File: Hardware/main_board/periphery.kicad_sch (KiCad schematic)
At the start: 0 parts

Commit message: sch: done periphery
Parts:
- added C80: 100nF, symbol Device:C
- added C81: TBD, symbol Device:C_Polarized_US
- added D10: LED_ABGR, symbol Device:LED_ABGR
- added D11, D12, D13, D14, D15, D16, D17, D18, D19, D20, D21, D22, D23, D24, D25, D26, D27, D28, D29, D30, D31: TVS, symbol Device:D_TVS
- added D32: 1N4148, symbol Device:D
- added F1: 2A, symbol Device:Polyfuse
- added J4: SD, symbol Connector:Micro_SD_Card_Det1
- added J5: EXT0, symbol Connector_Generic:Conn_01x08
- added J6: EXT1, symbol Connector_Generic:Conn_01x10
- added J7: NFC, symbol Connector_Generic_MountingPin:Conn_01x18_MountingPin
- added R36, R37, R43, R44, R45, R46, R47: 47K, symbol Device:R_US
- added R38, R39: 150R, symbol Device:R_US
- added R40, R41, R42, R49: 51R, symbol Device:R_US
- added R48: 0R, symbol Device:R_US
- added R50: 1K, symbol Device:R_US
- added RN1, RN2, RN3, RN4: 51R, symbol Library:R_Park
- added TP34: SWCLK, symbol Connector:TestPoint
- added TP35: SWDIO, symbol Connector:TestPoint
- added TP36: UART1_TX, symbol Connector:TestPoint
- added TP37: UART1_RX, symbol Connector:TestPoint
- added TP38: I2C2_SCL, symbol Connector:TestPoint
- added TP39: I2C2_SDA, symbol Connector:TestPoint
- added TP40: RFID_C, symbol Connector:TestPoint
- added TP41: IR_RX, symbol Connector:TestPoint
- added TP42: IR_TX, symbol Connector:TestPoint
- added TP43: SP, symbol Connector:TestPoint
- added TP44: iBTN, symbol Connector:TestPoint
- added TP45: RFID_O, symbol Connector:TestPoint
- added TP46: RFID_P, symbol Connector:TestPoint
- added TP47: VIBRO, symbol Connector:TestPoint
- added TP48: NFC_CS, symbol Connector:TestPoint
- added TP49: RFID_I, symbol Connector:TestPoint
- added U11: LP5562TMX, symbol Library:LP5562TMX
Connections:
- new net: J4.3 (CMD), R40.2
- new net: J4.1 (DAT2), R37.1
- new net: J4.2 (DAT3/CD), R39.2
- new net: D16.1 (A1), J4.4 (VDD), R36.2, R37.2, R43.2, R44.2, R45.2, R46.2, R47.2, R48.2
- new net: J4.5 (CLK), R41.2
- new net: J4.7 (DAT0), R42.2
- new net: J4.8 (DAT1), R36.1
- new net: J4.9 (DET), R38.2
- new net: J6.2 (Pin_2), RN3.3
- new net: J6.3 (Pin_3), RN3.2
- new net: J6.5 (Pin_5), RN3.1
- new net: J6.6 (Pin_6), RN4.4
- new net: J6.7 (Pin_7), RN4.3
- new net: J6.8 (Pin_8), RN4.2
- new net: J6.9 (Pin_9), RN4.1
- new net: C81.1, F1.2, J5.1 (Pin_1)
- new net: J5.2 (Pin_2), RN1.2
- new net: J5.3 (Pin_3), RN1.1
- new net: J5.4 (Pin_4), RN2.4
- new net: J5.5 (Pin_5), RN2.3
- new net: J5.6 (Pin_6), RN2.2
- new net: J5.7 (Pin_7), RN2.1
- new net: J7.9 (Pin_9), R49.2
- new net: D32.1 (K), R50.1
- new net: D10.2 (BK), U11.A4 (B)
- new net: D10.3 (GK), U11.B4 (G)
- new net: D10.4 (RK), U11.C4 (R)
- new net +3.3V: J7.3 (Pin_3)
- new net +3.3V_EXT: D24.2 (A2), J6.1 (Pin_1), R48.1
- new net GND: C80.2, C81.2, D11.2 (A2), D12.2 (A2), D13.2 (A2), D14.2 (A2), D15.2 (A2), D16.2 (A2), D17.2 (A2), D18.2 (A2), D19.2 (A2), D20.2 (A2), D21.2 (A2), D22.2 (A2), D23.2 (A2), D24.1 (A1), D25.2 (A2), D26.2 (A2), D27.2 (A2), D28.2 (A2), D29.2 (A2), D30.2 (A2), D31.2 (A2), J4.10 (SHIELD), J4.6 (VSS), J5.8 (Pin_8), J6.10 (Pin_10), J6.4 (Pin_4), J7.6 (Pin_6), J7.8 (Pin_8), J7.MP (MountPin), U11.A3 (CLK_32K), U11.B1 (A1), U11.B2 (A0), U11.B3 (GND)
- new net I2C_SCL: U11.C2 (SCL)
- new net I2C_SDA: U11.C1 (SDA)
- new net IR_RX: J7.17 (Pin_17), TP41.1
- new net IR_TX: J7.16 (Pin_16), TP42.1
- new net LCD_LED: U11.A1 (W)
- new net NFC_CS: J7.4 (Pin_4), TP48.1
- new net PA4: D19.1 (A1), RN2.8
- new net PA6: D18.1 (A1), RN1.5
- new net PA7: D17.1 (A1), RN1.6
- new net PB2: D21.1 (A1), RN2.6
- new net PB3: D20.1 (A1), RN2.7
- new net PC0: D30.1 (A1), RN4.6, TP38.1
- new net PC1: D29.1 (A1), RN4.7, TP39.1
- new net PC3: D22.1 (A1), RN2.5
- new net RESET: U11.C3 (EN_VCC)
- new net RFID_CARRIER: J7.18 (Pin_18), TP40.1
- new net RFID_OUT: J7.12 (Pin_12), TP45.1
- new net RFID_PULL: J7.11 (Pin_11), TP46.1
- new net RFID_RF_IN: J7.5 (Pin_5), TP49.1
- new net SD_CD: D15.1 (A1), R38.1, R47.1
- new net SD_CS: D11.1 (A1), R39.1, R43.1
- new net SPEAKER: J7.15 (Pin_15), TP43.1
- new net SPI_D_MISO: D14.1 (A1), R42.1, R46.1
- new net SPI_D_MOSI: D12.1 (A1), R40.1, R44.1
- new net SPI_D_SCK: D13.1 (A1), R41.1, R45.1
- new net SPI_R_MISO: R49.1
- new net SPI_R_MOSI: J7.13 (Pin_13)
- new net SPI_R_SCK: J7.7 (Pin_7)
- new net SWCLK: D25.1 (A1), RN3.7, TP34.1
- new net SWDIO: D26.1 (A1), RN3.6, TP35.1
- new net UART1_RX: D28.1 (A1), RN4.8, TP37.1
- new net UART1_TX: D27.1 (A1), RN3.5, TP36.1
- new net VIBRO: J7.10 (Pin_10), TP47.1
- new net VSYS: C80.1, D10.1 (A), U11.A2 (VDD)
- new net VUSB: D23.1 (A1), D32.2 (A), F1.1, J7.1 (Pin_1), J7.2 (Pin_2)
- new net iBTN: D31.1 (A1), J7.14 (Pin_14), R50.2, RN4.5, TP44.1
- no-connect marks 0 -> 6
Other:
- note added: "EXT PORT"
- note added: "LED"
- note added: "NFC BOARD"
- note added: "SD"

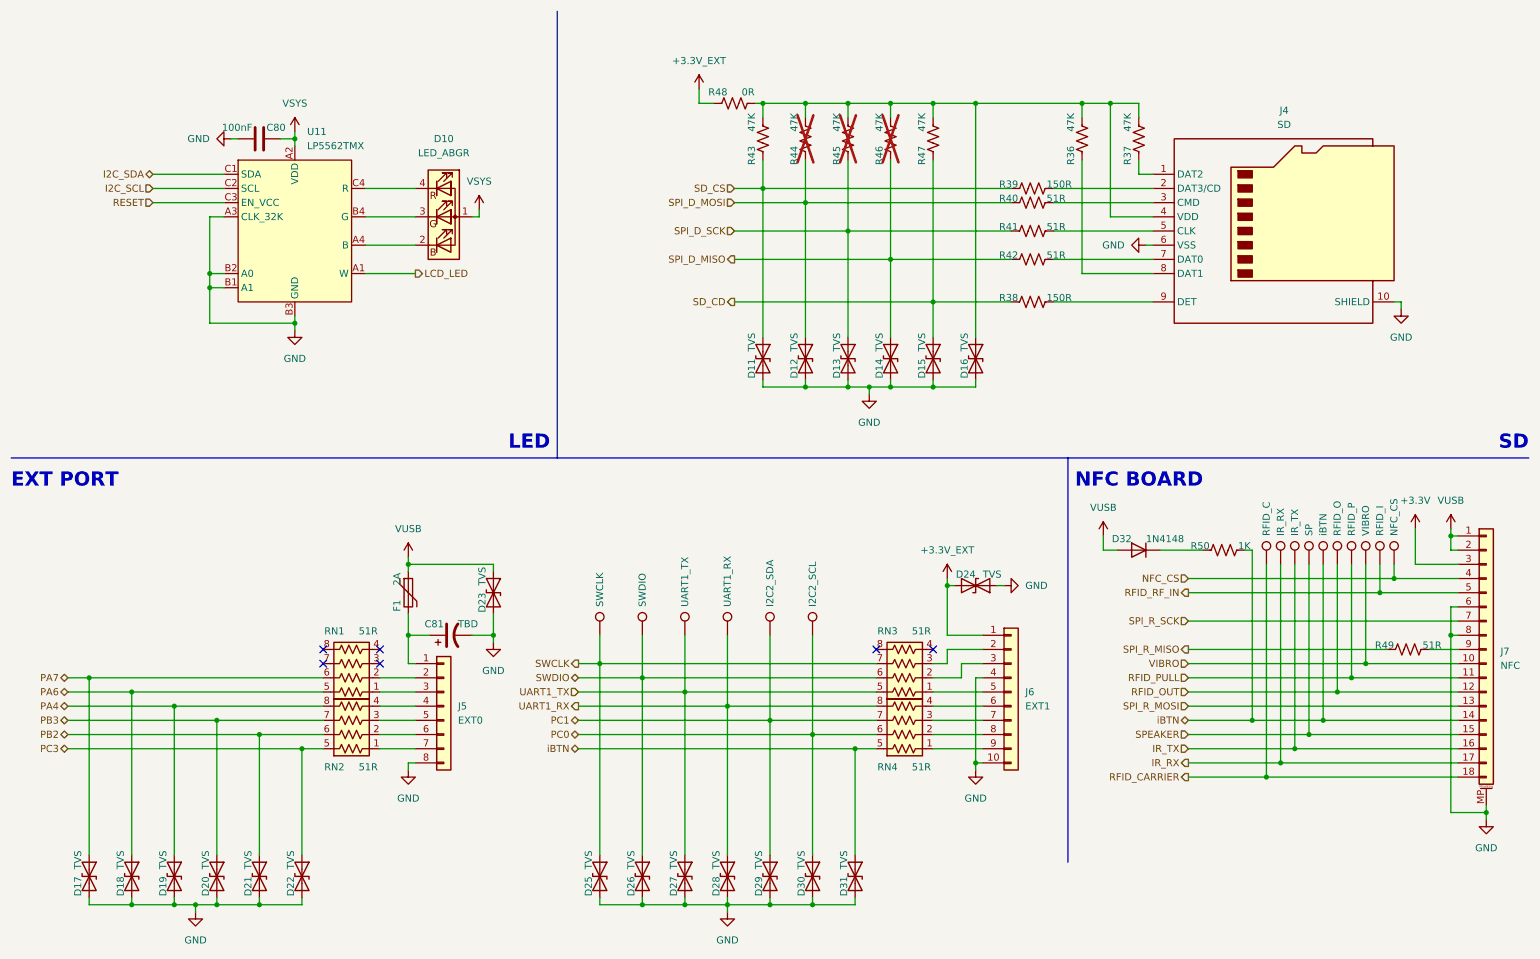
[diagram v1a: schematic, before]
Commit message: sch: add some part of footprints
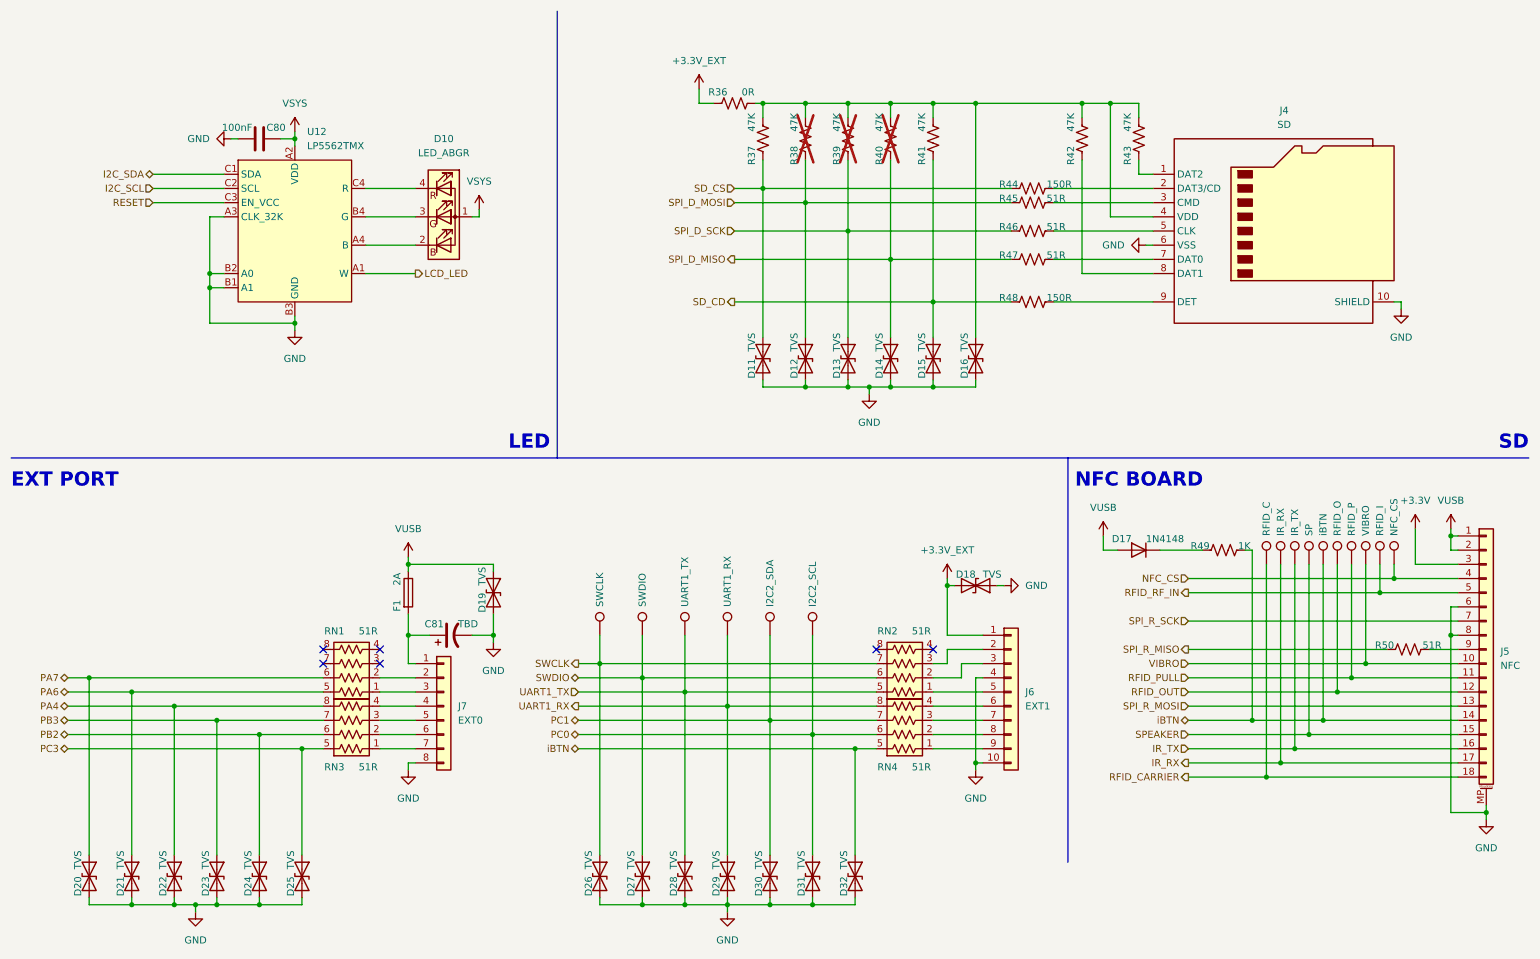
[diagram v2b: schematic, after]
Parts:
- C80: footprint (none) -> Capacitor_SMD:C_0402_1005Metric
- C81: footprint (none) -> Capacitor_SMD:C_1206_3216Metric
- D11, D12, D13, D14, D15, D16: footprint (none) -> Diode_SMD:D_0201_0603Metric
- D17: renamed from D32; footprint (none) -> Diode_SMD:D_SOD-523
- D18: renamed from D24; footprint (none) -> Diode_SMD:D_0201_0603Metric
- D19: renamed from D23; footprint (none) -> Diode_SMD:D_0201_0603Metric
- D20: renamed from D17; footprint (none) -> Diode_SMD:D_0201_0603Metric
- D21: renamed from D18; footprint (none) -> Diode_SMD:D_0201_0603Metric
- D22: renamed from D19; footprint (none) -> Diode_SMD:D_0201_0603Metric
- D23: renamed from D20; footprint (none) -> Diode_SMD:D_0201_0603Metric
- D24: renamed from D21; footprint (none) -> Diode_SMD:D_0201_0603Metric
- D25: renamed from D22; footprint (none) -> Diode_SMD:D_0201_0603Metric
- D26: renamed from D25; footprint (none) -> Diode_SMD:D_0201_0603Metric
- D27: renamed from D26; footprint (none) -> Diode_SMD:D_0201_0603Metric
- D28: renamed from D27; footprint (none) -> Diode_SMD:D_0201_0603Metric
- D29: renamed from D28; footprint (none) -> Diode_SMD:D_0201_0603Metric
- D30: renamed from D29; footprint (none) -> Diode_SMD:D_0201_0603Metric
- D31: renamed from D30; footprint (none) -> Diode_SMD:D_0201_0603Metric
- D32: renamed from D31; footprint (none) -> Diode_SMD:D_0201_0603Metric
- F1: footprint (none) -> Fuse:Fuse_0402_1005Metric; symbol Device:Polyfuse -> Device:Fuse
- J4: footprint (none) -> Connector_Card:microSD_HC_Molex_104031-0811
- R36: renamed from R48; footprint (none) -> Resistor_SMD:R_0402_1005Metric
- R37: renamed from R43; footprint (none) -> Resistor_SMD:R_0402_1005Metric
- R38: renamed from R44; footprint (none) -> Resistor_SMD:R_0402_1005Metric
- R39: renamed from R45; footprint (none) -> Resistor_SMD:R_0402_1005Metric
- R40: renamed from R46; footprint (none) -> Resistor_SMD:R_0402_1005Metric
- R41: renamed from R47; footprint (none) -> Resistor_SMD:R_0402_1005Metric
- R42: renamed from R36; footprint (none) -> Resistor_SMD:R_0402_1005Metric
- R43: renamed from R37; footprint (none) -> Resistor_SMD:R_0402_1005Metric
- R44: renamed from R39; footprint (none) -> Resistor_SMD:R_0402_1005Metric
- R45: renamed from R40; footprint (none) -> Resistor_SMD:R_0402_1005Metric
- R46: renamed from R41; footprint (none) -> Resistor_SMD:R_0402_1005Metric
- R47: renamed from R42; footprint (none) -> Resistor_SMD:R_0402_1005Metric
- R48: renamed from R38; footprint (none) -> Resistor_SMD:R_0402_1005Metric
- R49: renamed from R50; footprint (none) -> Resistor_SMD:R_0402_1005Metric
- R50: renamed from R49; footprint (none) -> Resistor_SMD:R_0402_1005Metric
- RN1, RN4: footprint (none) -> Resistor_SMD:R_Array_Concave_4x0402
- RN2: renamed from RN3; footprint (none) -> Resistor_SMD:R_Array_Concave_4x0402
- RN3: renamed from RN2; footprint (none) -> Resistor_SMD:R_Array_Concave_4x0402
- TP34: renamed from TP40; footprint (none) -> TestPoint:TestPoint_Pad_D1.0mm
- TP35: renamed from TP41; footprint (none) -> TestPoint:TestPoint_Pad_D1.0mm
- TP36: renamed from TP42; footprint (none) -> TestPoint:TestPoint_Pad_D1.0mm
- TP37: renamed from TP43; footprint (none) -> TestPoint:TestPoint_Pad_D1.0mm
- TP38: renamed from TP44; footprint (none) -> TestPoint:TestPoint_Pad_D1.0mm
- TP39: renamed from TP45; footprint (none) -> TestPoint:TestPoint_Pad_D1.0mm
- TP40: renamed from TP46; footprint (none) -> TestPoint:TestPoint_Pad_D1.0mm
- TP41: renamed from TP47; footprint (none) -> TestPoint:TestPoint_Pad_D1.0mm
- TP42: renamed from TP49; footprint (none) -> TestPoint:TestPoint_Pad_D1.0mm
- TP43: renamed from TP48; footprint (none) -> TestPoint:TestPoint_Pad_D1.0mm
- TP44: renamed from TP34; footprint (none) -> TestPoint:TestPoint_Pad_D1.0mm
- TP45: renamed from TP35; footprint (none) -> TestPoint:TestPoint_Pad_D1.0mm
- TP46: renamed from TP36; footprint (none) -> TestPoint:TestPoint_Pad_D1.0mm
- TP47: renamed from TP37; footprint (none) -> TestPoint:TestPoint_Pad_D1.0mm
- TP48: renamed from TP39; footprint (none) -> TestPoint:TestPoint_Pad_D1.0mm
- TP49: renamed from TP38; footprint (none) -> TestPoint:TestPoint_Pad_D1.0mm
- renumbered J7 to J5, J5 to J7, U11 to U12

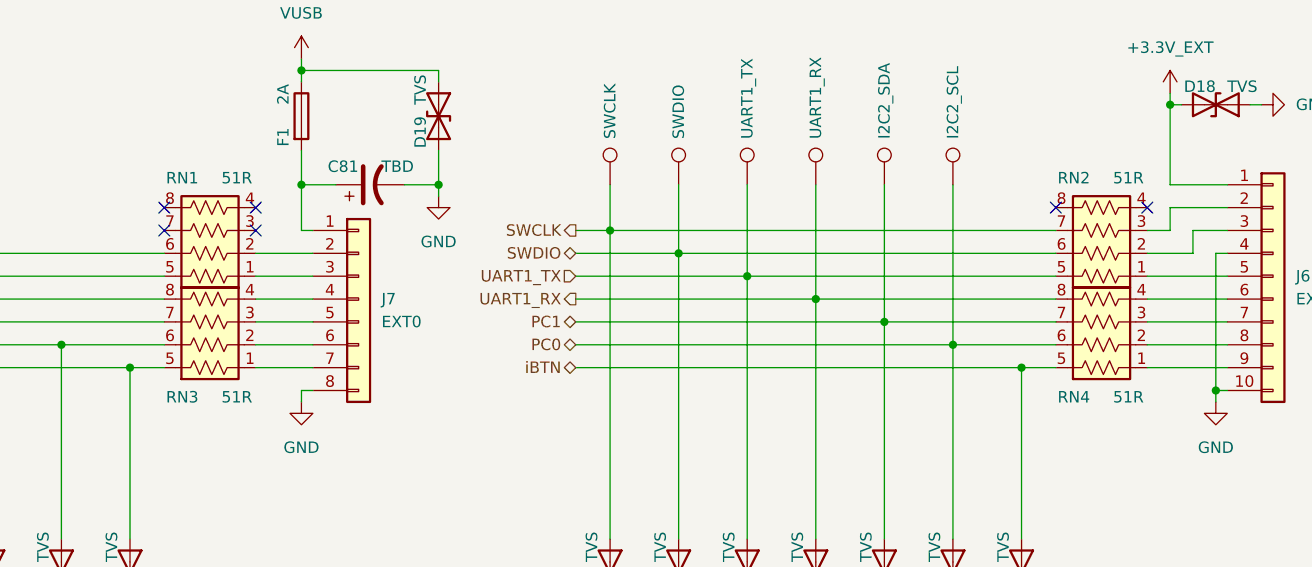
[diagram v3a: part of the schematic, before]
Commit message: layout: change some of the footprint and start to layout
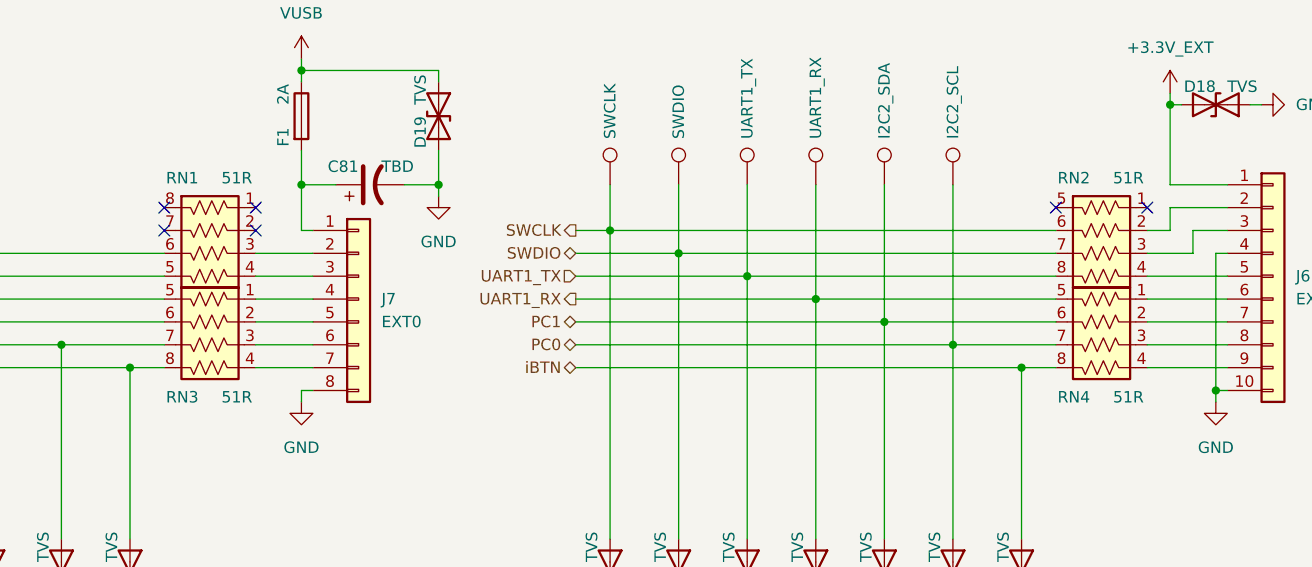
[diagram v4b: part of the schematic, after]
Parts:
- C81: footprint Capacitor_SMD:C_1206_3216Metric -> Capacitor_Tantalum_SMD:CP_EIA-3216-18_Kemet-A
- D10: footprint (none) -> Library:LED_PLCC-4_1.5x1.5mm_CW
- J4: footprint Connector_Card:microSD_HC_Molex_104031-0811 -> Library:TF_C393941
- J5: footprint (none) -> Library:CONN18x1_FH34SRJ-18S-0.5SH50_HIR
- J6: footprint (none) -> Library:PinSocket_1x10_P2.54mm_Horizontal_SMD
- J7: footprint (none) -> Library:PinSocket_1x08_P2.54mm_Horizontal_SMD
- U12: footprint (none) -> Library:BGA-12_4x3_1.6x1.2mm
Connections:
- net PA4: now also RN3.5; no longer RN3.8
- net PB2: now also RN3.7; no longer RN3.6
- net PB3: now also RN3.6; no longer RN3.7
- net PC0: now also RN4.7; no longer RN4.6
- net PC1: now also RN4.6; no longer RN4.7
- net PC3: now also RN3.8; no longer RN3.5
- net SWCLK: now also RN2.6; no longer RN2.7
- net SWDIO: now also RN2.7; no longer RN2.6
- net UART1_RX: now also RN4.5; no longer RN4.8
- net UART1_TX: now also RN2.8; no longer RN2.5
- net iBTN: now also RN4.8; no longer RN4.5
- net at J6.2 (Pin_2): now also RN2.2; no longer RN2.3
- net at J6.3 (Pin_3): now also RN2.3; no longer RN2.2
- net at J6.5 (Pin_5): now also RN2.4; no longer RN2.1
- net at J6.6 (Pin_6): now also RN4.1; no longer RN4.4
- net at J6.7 (Pin_7): now also RN4.2; no longer RN4.3
- net at J6.8 (Pin_8): now also RN4.3; no longer RN4.2
- net at J6.9 (Pin_9): now also RN4.4; no longer RN4.1
- net at J7.2 (Pin_2): now also RN1.3; no longer RN1.2
- net at J7.3 (Pin_3): now also RN1.4; no longer RN1.1
- net at J7.4 (Pin_4): now also RN3.1; no longer RN3.4
- net at J7.5 (Pin_5): now also RN3.2; no longer RN3.3
- net at J7.6 (Pin_6): now also RN3.3; no longer RN3.2
- net at J7.7 (Pin_7): now also RN3.4; no longer RN3.1
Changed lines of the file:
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@@
 			)
 		)
-		(property "Footprint" "Connector_Card:microSD_HC_Molex_104031-0811"
+		(property "Footprint" "Library:TF_C393941"
 			(at 292.1 34.29 0)
 			(effects
@@
 			)
 		)
-		(property "Footprint" ""
+		(property "Footprint" "Library:PinSocket_1x10_P2.54mm_Horizontal_SMD"
 			(at 191.77 134.62 0)
 			(effects
@@
 			)
 		)
-		(property "Footprint" ""
+		(property "Footprint" "Library:PinSocket_1x08_P2.54mm_Horizontal_SMD"
 			(at 90.17 137.16 0)
 			(effects
@@
 		(lib_id "Library:R_Park")
 		(at 172.72 130.81 90)
+		(mirror x)
 		(unit 1)
 		(exclude_from_sim no)
@@
 					(size 1.27 1.27)
 				)
-				(justify left top)
+				(justify left bottom)
 			)
 		)
@@
 					(size 1.27 1.27)
 				)
-				(justify right top)
+				(justify right bottom)
 			)
 		)
@@
 			)
 		)
-		(property "Footprint" "Capacitor_SMD:C_1206_3216Metric"
+		(property "Footprint" "Capacitor_Tantalum_SMD:CP_EIA-3216-18_Kemet-A"
 			(at 91.44 124.46 0)
 			(effects
@@
 	)
 	(symbol
+		(lib_name "R_Park_1")
 		(lib_id "Library:R_Park")
 		(at 73.66 130.81 90)
+		(mirror x)
 		(unit 1)
 		(exclude_from_sim no)
@@
 					(size 1.27 1.27)
 				)
-				(justify left top)
+				(justify left bottom)
 			)
 		)
@@
 					(size 1.27 1.27)
 				)
-				(justify right top)
+				(justify right bottom)
 			)
 		)
@@
 		(lib_id "Library:R_Park")
 		(at 73.66 140.97 90)
+		(mirror x)
 		(unit 1)
 		(exclude_from_sim no)
@@
 					(size 1.27 1.27)
 				)
-				(justify left bottom)
+				(justify left top)
 			)
 		)
@@
 					(size 1.27 1.27)
 				)
-				(justify right bottom)
+				(justify right top)
 			)
 		)
@@
 			)
 		)
-		(property "Footprint" ""
+		(property "Footprint" "Library:BGA-12_4x3_1.6x1.2mm"
 			(at 69.85 35.56 0)
 			(effects
@@
 		(lib_id "Library:R_Park")
 		(at 172.72 140.97 90)
+		(mirror x)
 		(unit 1)
 		(exclude_from_sim no)
@@
 					(size 1.27 1.27)
 				)
-				(justify left bottom)
+				(justify left top)
 			)
 		)
@@
 					(size 1.27 1.27)
 				)
-				(justify right bottom)
+				(justify right top)
 			)
 		)
@@
 			)
 		)
-		(property "Footprint" ""
+		(property "Footprint" "Library:CONN18x1_FH34SRJ-18S-0.5SH50_HIR"
 			(at 276.86 127 0)
 			(effects
@@
 			)
 		)
-		(property "Footprint" ""
+		(property "Footprint" "Library:LED_PLCC-4_1.5x1.5mm_CW"
 			(at 90.17 50.8 0)
 			(effects
